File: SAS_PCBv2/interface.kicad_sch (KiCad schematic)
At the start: 0 parts

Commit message: Added basic Buttons w/ Rpi connections
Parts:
- added C3, C4, C5, C6, C7, C8: 100nF, symbol Device:C
- added J4, J5, J6, J7, J8, J9: Conn_01x02, symbol Connector_Generic:Conn_01x02
- added R2, R3, R4, R5, R6, R7: 33k, symbol Device:R
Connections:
- new net +3V3: R2.1, R3.1, R4.1, R5.1, R6.1, R7.1
- new net BTN_1: C3.1, J4.1 (Pin_1), R2.2
- new net BTN_2: C4.1, J5.1 (Pin_1), R3.2
- new net BTN_3: C5.1, J6.1 (Pin_1), R4.2
- new net BTN_4: C6.1, J7.1 (Pin_1), R5.2
- new net BTN_5: C7.1, J8.1 (Pin_1), R6.2
- new net BTN_6: C8.1, J9.1 (Pin_1), R7.2
- new net GND: C3.2, C4.2, C5.2, C6.2, C7.2, C8.2, J4.2 (Pin_2), J5.2 (Pin_2), J6.2 (Pin_2), J7.2 (Pin_2), J8.2 (Pin_2), J9.2 (Pin_2)
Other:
- note added: "Basic Buttons"

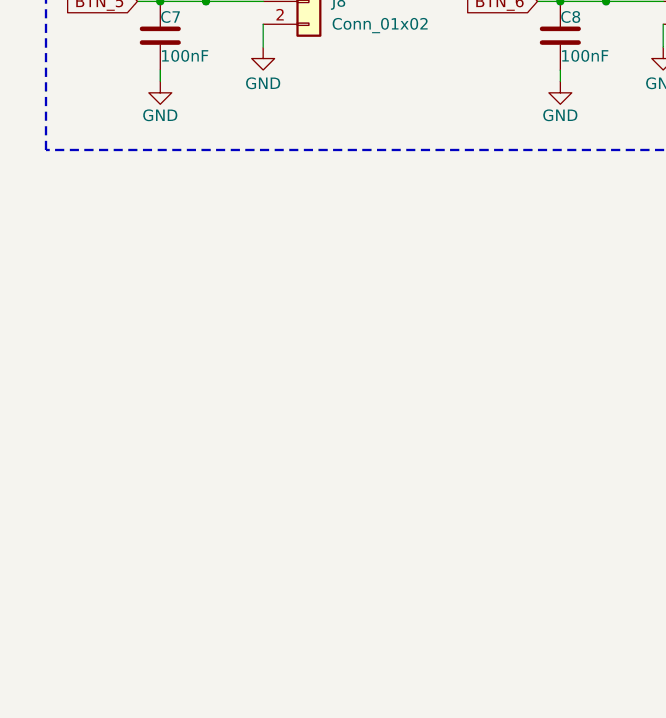
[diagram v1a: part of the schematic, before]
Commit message: Added secondary displays, completed LDO 3V3
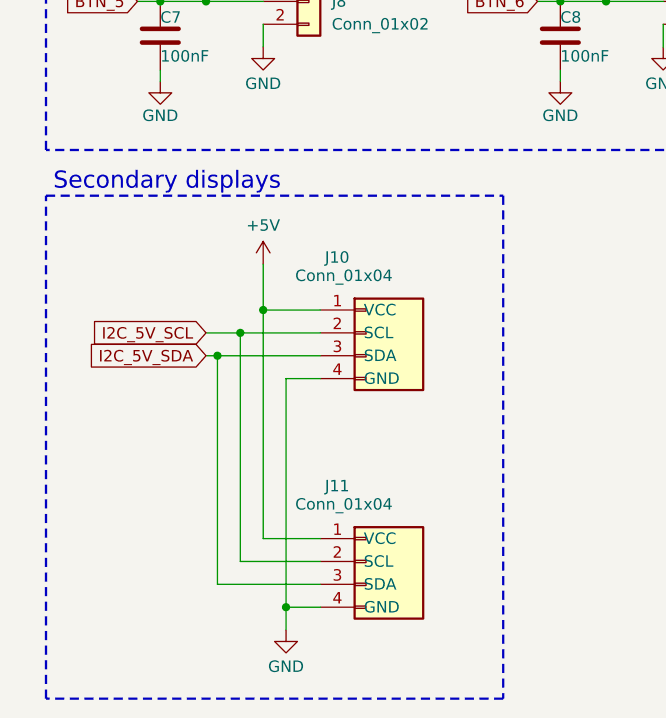
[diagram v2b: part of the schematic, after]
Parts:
- added J10, J11: Conn_01x04, symbol Connector_Generic:Conn_01x04
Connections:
- net GND: now also J10.4 (GND), J11.4 (GND)
- new net +5V: J10.1 (VCC), J11.1 (VCC)
- new net I2C_5V_SCL: J10.2 (SCL), J11.2 (SCL)
- new net I2C_5V_SDA: J10.3 (SDA), J11.3 (SDA)
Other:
- note added: "Secondary displays"

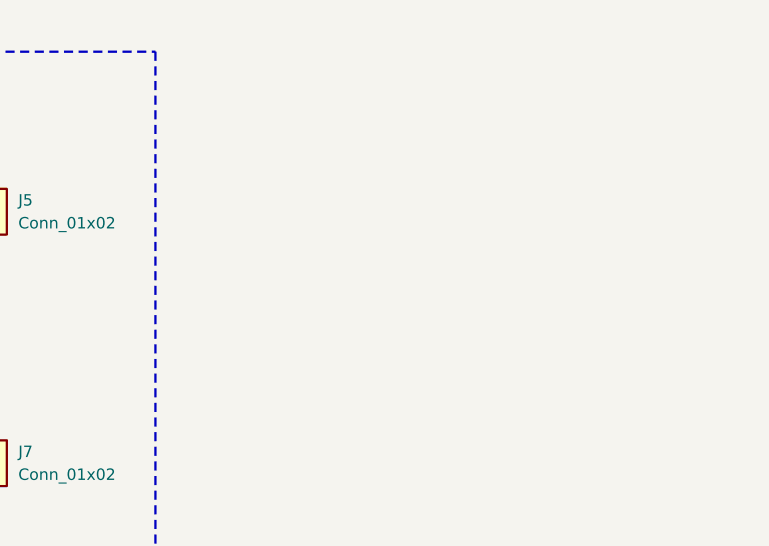
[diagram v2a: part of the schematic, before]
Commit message: Radio et GPS fait selon les datasheets normalement
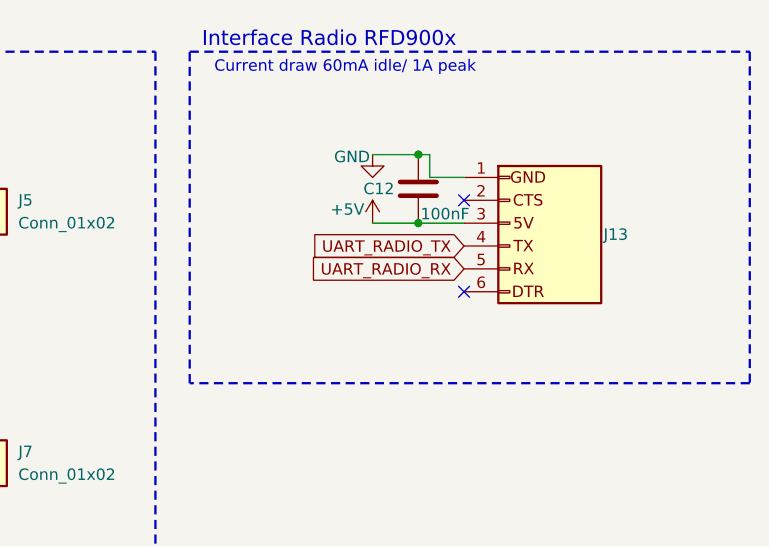
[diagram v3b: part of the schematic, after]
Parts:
- added C12: 100nF, symbol Device:C
- added J13: Adatateur FTDI (Radio RFD900x), symbol Connector_Generic:Conn_01x06
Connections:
- net +5V: now also C12.2, J13.3 (5V)
- net GND: now also C12.1, J13.1 (GND)
- new net UART_RADIO_RX: J13.5 (RX)
- new net UART_RADIO_TX: J13.4 (TX)
- no-connect marks 0 -> 2
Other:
- note added: "Current draw 60mA idle/ 1A peak"
- note added: "Interface Radio RFD900x"

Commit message: schematic sans error et le debut de pcb
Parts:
- C12, C3, C4, C5, C6, C7, C8: footprint (none) -> Capacitor_THT:C_Disc_D5.0mm_W2.5mm_P2.50mm
- J10, J11: footprint (none) -> Connector_PinHeader_2.54mm:PinHeader_1x04_P2.54mm_Vertical
- J13: footprint (none) -> Connector_PinHeader_2.54mm:PinHeader_1x06_P2.54mm_Vertical
- J4, J5, J6, J7, J8, J9: footprint (none) -> Connector_PinHeader_2.54mm:PinHeader_1x02_P2.54mm_Vertical
- R2, R3, R4, R5, R6, R7: footprint (none) -> Resistor_THT:R_Axial_DIN0207_L6.3mm_D2.5mm_P10.16mm_Horizontal
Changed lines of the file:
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@@
 			)
 		)
-		(property "Footprint" ""
+		(property "Footprint" "Connector_PinHeader_2.54mm:PinHeader_1x02_P2.54mm_Vertical"
 			(at 44.45 90.17 0)
 			(effects
@@
 			)
 		)
-		(property "Footprint" ""
+		(property "Footprint" "Capacitor_THT:C_Disc_D5.0mm_W2.5mm_P2.50mm"
 			(at 28.9052 41.91 0)
 			(effects
@@
 			)
 		)
-		(property "Footprint" ""
+		(property "Footprint" "Connector_PinHeader_2.54mm:PinHeader_1x06_P2.54mm_Vertical"
 			(at 146.05 36.83 0)
 			(effects
@@
 			)
 		)
-		(property "Footprint" ""
+		(property "Footprint" "Capacitor_THT:C_Disc_D5.0mm_W2.5mm_P2.50mm"
 			(at 136.8552 36.83 0)
 			(effects
@@
 			)
 		)
-		(property "Footprint" ""
+		(property "Footprint" "Connector_PinHeader_2.54mm:PinHeader_1x02_P2.54mm_Vertical"
 			(at 44.45 62.23 0)
 			(effects
@@
 			)
 		)
-		(property "Footprint" ""
+		(property "Footprint" "Connector_PinHeader_2.54mm:PinHeader_1x02_P2.54mm_Vertical"
 			(at 44.45 34.29 0)
 			(effects
@@
 			)
 		)
-		(property "Footprint" ""
+		(property "Footprint" "Resistor_THT:R_Axial_DIN0207_L6.3mm_D2.5mm_P10.16mm_Horizontal"
 			(at 75.692 58.42 90)
 			(effects
@@
 			)
 		)
-		(property "Footprint" ""
+		(property "Footprint" "Connector_PinHeader_2.54mm:PinHeader_1x04_P2.54mm_Vertical"
 			(at 50.8 152.4 0)
 			(effects
@@
 			)
 		)
-		(property "Footprint" ""
+		(property "Footprint" "Capacitor_THT:C_Disc_D5.0mm_W2.5mm_P2.50mm"
 			(at 28.9052 69.85 0)
 			(effects
@@
 			)
 		)
-		(property "Footprint" ""
+		(property "Footprint" "Connector_PinHeader_2.54mm:PinHeader_1x02_P2.54mm_Vertical"
 			(at 88.9 34.29 0)
 			(effects
@@
 			)
 		)
-		(property "Footprint" ""
+		(property "Footprint" "Capacitor_THT:C_Disc_D5.0mm_W2.5mm_P2.50mm"
 			(at 73.3552 97.79 0)
 			(effects
@@
 			)
 		)
-		(property "Footprint" ""
+		(property "Footprint" "Resistor_THT:R_Axial_DIN0207_L6.3mm_D2.5mm_P10.16mm_Horizontal"
 			(at 31.242 30.48 90)
 			(effects
@@
 			)
 		)
-		(property "Footprint" ""
+		(property "Footprint" "Resistor_THT:R_Axial_DIN0207_L6.3mm_D2.5mm_P10.16mm_Horizontal"
 			(at 75.692 30.48 90)
 			(effects
@@
 			)
 		)
-		(property "Footprint" ""
+		(property "Footprint" "Resistor_THT:R_Axial_DIN0207_L6.3mm_D2.5mm_P10.16mm_Horizontal"
 			(at 31.242 58.42 90)
 			(effects
@@
 			)
 		)
-		(property "Footprint" ""
+		(property "Footprint" "Resistor_THT:R_Axial_DIN0207_L6.3mm_D2.5mm_P10.16mm_Horizontal"
 			(at 75.692 86.36 90)
 			(effects
@@
 			)
 		)
-		(property "Footprint" ""
+		(property "Footprint" "Capacitor_THT:C_Disc_D5.0mm_W2.5mm_P2.50mm"
 			(at 28.9052 97.79 0)
 			(effects
@@
 			)
 		)
-		(property "Footprint" ""
+		(property "Footprint" "Resistor_THT:R_Axial_DIN0207_L6.3mm_D2.5mm_P10.16mm_Horizontal"
 			(at 31.242 86.36 90)
 			(effects
@@
 			)
 		)
-		(property "Footprint" ""
+		(property "Footprint" "Connector_PinHeader_2.54mm:PinHeader_1x04_P2.54mm_Vertical"
 			(at 50.8 127 0)
 			(effects
@@
 			)
 		)
-		(property "Footprint" ""
+		(property "Footprint" "Connector_PinHeader_2.54mm:PinHeader_1x02_P2.54mm_Vertical"
 			(at 88.9 90.17 0)
 			(effects
@@
 			)
 		)
-		(property "Footprint" ""
+		(property "Footprint" "Capacitor_THT:C_Disc_D5.0mm_W2.5mm_P2.50mm"
 			(at 73.3552 69.85 0)
 			(effects
@@
 			)
 		)
-		(property "Footprint" ""
+		(property "Footprint" "Capacitor_THT:C_Disc_D5.0mm_W2.5mm_P2.50mm"
 			(at 73.3552 41.91 0)
 			(effects
@@
 			)
 		)
-		(property "Footprint" ""
+		(property "Footprint" "Connector_PinHeader_2.54mm:PinHeader_1x02_P2.54mm_Vertical"
 			(at 88.9 62.23 0)
 			(effects

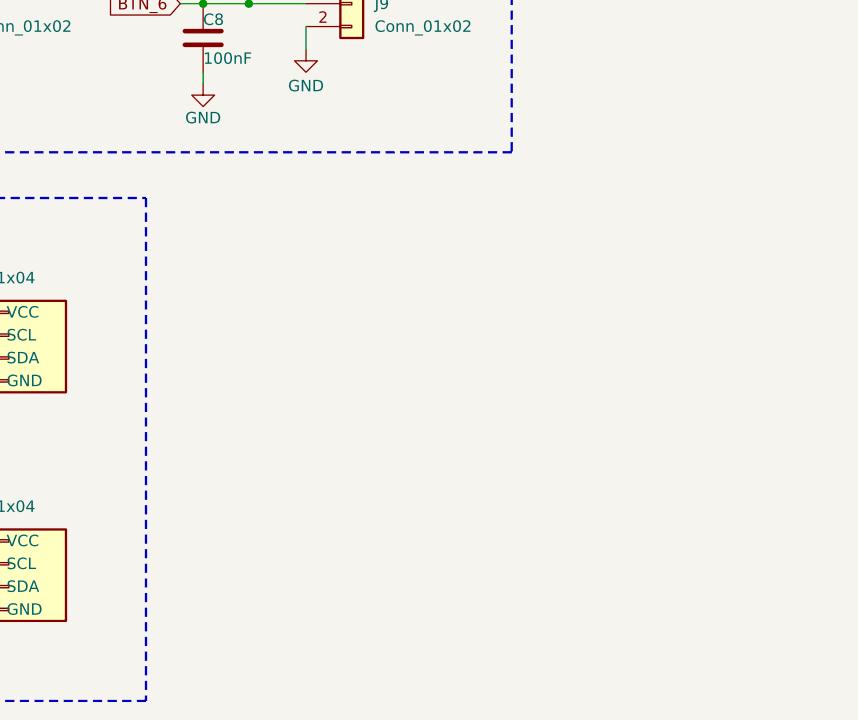
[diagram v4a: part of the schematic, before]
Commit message: Correction UART5 -> UART3, ajout d'un ventilateur 12V PWM
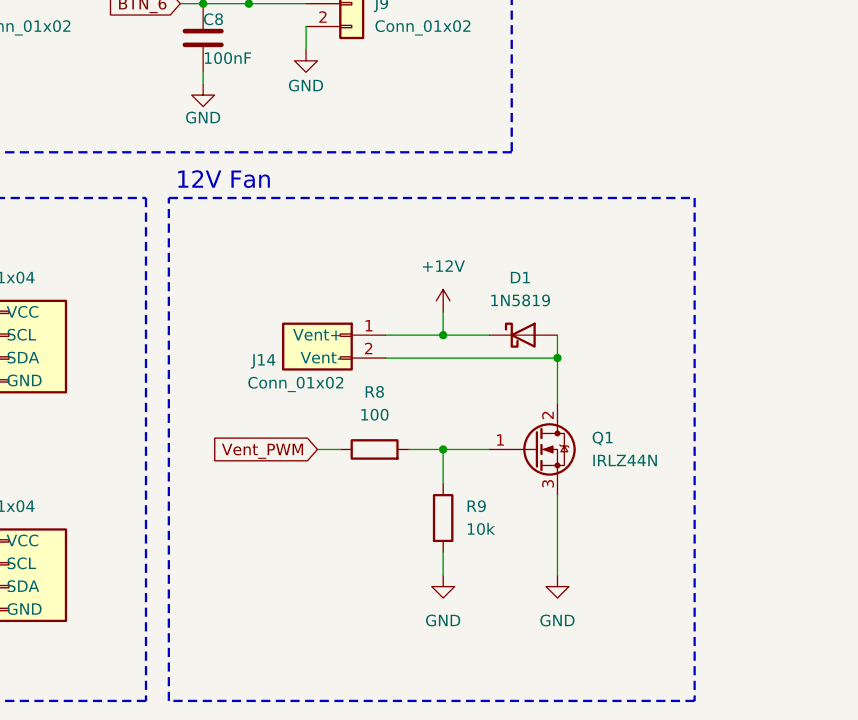
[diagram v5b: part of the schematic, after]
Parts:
- added D1: 1N5819, Diode_THT:D_DO-41_SOD81_P10.16mm_Horizontal, symbol Diode:1N5819
- added J14: Conn_01x02, Connector_PinHeader_2.54mm:PinHeader_1x02_P2.54mm_Vertical, symbol Connector_Generic:Conn_01x02
- added Q1: IRLZ44N, Package_TO_SOT_THT:TO-220-3_Vertical, symbol Transistor_FET:IRLZ44N
- added R8: 100, symbol Device:R
- added R9: 10k, symbol Device:R
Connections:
- net GND: now also Q1.3 (S), R9.2
- new net: Q1.1 (G), R8.2, R9.1
- new net: D1.2 (A), J14.2 (Vent-), Q1.2 (D)
- new net +12V: D1.1 (K), J14.1 (Vent+)
- new net Vent_PWM: R8.1
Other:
- note added: "12V Fan"

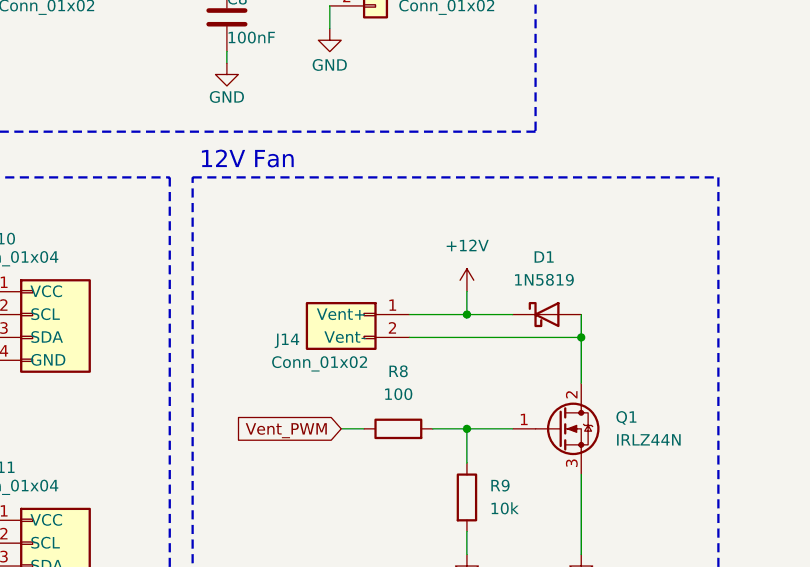
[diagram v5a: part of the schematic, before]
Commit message: Switch USB/PCB, connections Power, spam condensateurs, resistance pull-up
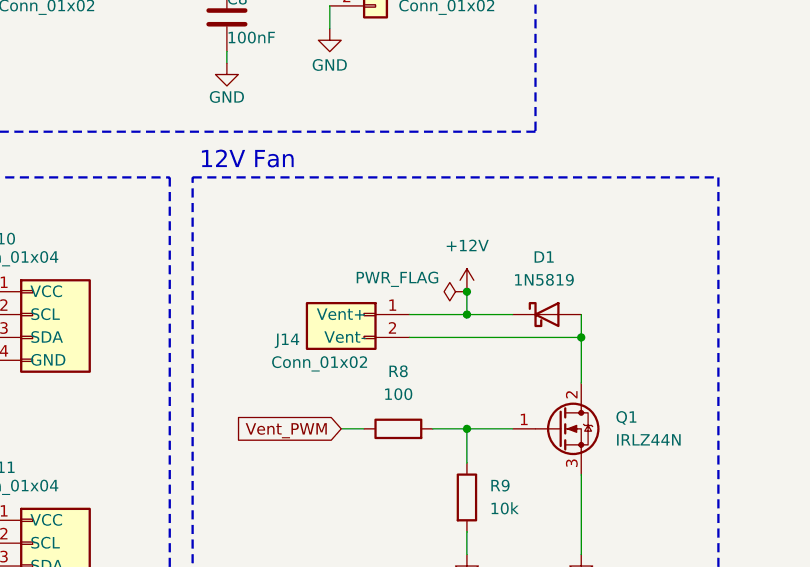
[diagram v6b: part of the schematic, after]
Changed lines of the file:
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@@
 	)
 	(junction
+		(at 99.06 124.46)
+		(diameter 0)
+		(color 0 0 0 0)
+	)
+	(junction
 		(at 77.47 90.17)
 		(diameter 0)
@@
 					(unit 1)
 				)
+			)
+		)
+	)
+	(symbol
+		(lib_id "power:PWR_FLAG")
+		(at 99.06 124.46 90)
+		(unit 1)
+		(exclude_from_sim no)
+		(in_bom yes)
+		(on_board yes)
+		(dnp no)
+		(property "Reference" "#FLG05"
+			(at 97.155 124.46 0)
+			(effects
+				(font
+					(size 1.27 1.27)
+				)
+				(hide yes)
+			)
+		)
+		(property "Value" "PWR_FLAG"
+			(at 96.012 122.936 90)
+			(effects
+				(font
+					(size 1.27 1.27)
+				)
+				(justify left)
+			)
+		)
+		(property "Footprint" ""
+			(at 99.06 124.46 0)
+			(effects
+				(font
+					(size 1.27 1.27)
+				)
+				(hide yes)
+			)
+		)
+		(property "Datasheet" "~"
+			(at 99.06 124.46 0)
+			(effects
+				(font
+					(size 1.27 1.27)
+				)
+				(hide yes)
+			)
+		)
+		(property "Description" "Special symbol for telling ERC where power comes from"
+			(at 99.06 124.46 0)
+			(effects
+				(font
+					(size 1.27 1.27)
+				)
+				(hide yes)
+			)
+		)
+		(pin "1"
+		)
+		(instances
+			(project "SAS_PCBv2"
+				(path "/9d66b581-dc57-43dc-b827-73e5c0cd12f6/f2a97dc0-fb9e-4683-8449-3158c449818f"
+					(reference "#FLG05")
+					(unit 1)
+				)

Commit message: LDO du service, Logic level shifter custom
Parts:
- added C18: 100nF, Capacitor_THT:C_Disc_D5.0mm_W2.5mm_P2.50mm, symbol Device:C
- added J15: Adatateur FTDI (Radio RFD900x), Connector_PinHeader_2.54mm:PinHeader_1x06_P2.54mm_Vertical, symbol Connector_Generic:Conn_01x06
- C3, C4, C5, C6, C7, C8: value 100nF -> 2.2uF
- R2, R3, R4, R5, R6, R7: value 33k -> 10k
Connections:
- net +12V is gone; now on net +5V: D1.1 (K), J14.1 (Vent+)
- net +5V: now also C18.2, J15.3 (5V)
- net GND: now also C18.1, J15.1 (GND)
- net UART_RADIO_RX renamed UART_RAD1_RX
- net UART_RADIO_TX renamed UART_RAD1_TX
- new net UART_RAD2_RX: J15.5 (RX)
- new net UART_RAD2_TX: J15.4 (TX)
- no-connect marks 2 -> 4
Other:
- note added: "5V Fan"
- note added: "Interface Radio RFD900x #1"
- note added: "Interface Radio RFD900x #2"
- note removed: "12V Fan"
- note removed: "Interface Radio RFD900x"
